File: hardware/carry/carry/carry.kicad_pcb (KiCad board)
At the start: 2 copper layers, 65 parts, among them J1 LEFT IN, J2 RIGHT IN, J3 LEFT OUT, J4 RIGHT OUT, J5 694106301002, J6 Conn_02x22_Odd_Even, J7 JST XH, U1 MCP6002-E/SN, U2 MCP6002-E/SN, U3 AZ1117CH2-5.0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

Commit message: routing carry board
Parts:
- added C26: 100n, Capacitor_SMD:C_0603_1608Metric, F.Cu at (113.0, 37.0)
- added C27: 100n, Capacitor_SMD:C_0603_1608Metric, F.Cu at (113.0, 44.0)
- added C28: 100n, Capacitor_SMD:C_0603_1608Metric, F.Cu at (132.0, 44.0)
- added H2: MountingHole_Pad, MountingHole:MountingHole_3.2mm_M3_Pad_Via, F.Cu at (44.0, 34.0)
- added H3: MountingHole_Pad, MountingHole:MountingHole_3.2mm_M3_Pad_Via, F.Cu at (136.0, 34.0)
- added H4: MountingHole_Pad, MountingHole:MountingHole_3.2mm_M3_Pad_Via, F.Cu at (136.0, 96.0)
- added H5: MountingHole_Pad, MountingHole:MountingHole_3.2mm_M3_Pad_Via, F.Cu at (44.0, 96.0)
- added J8: Conn_01x06, Connector_PinSocket_2.54mm:PinSocket_1x06_P2.54mm_Vertical, F.Cu at (83.0, 33.0)
- added R20: 100k, Resistor_SMD:R_0603_1608Metric, F.Cu at (114.0, 34.0)
- added R21: 100k, Resistor_SMD:R_0603_1608Metric, F.Cu at (112.0, 34.0)
- added R22: 100k, Resistor_SMD:R_0603_1608Metric, F.Cu at (114.0, 47.0)
- added R23: 100k, Resistor_SMD:R_0603_1608Metric, F.Cu at (112.0, 47.0)
- added R24: 100k, Resistor_SMD:R_0603_1608Metric, F.Cu at (131.0, 47.0)
- added R25: 100k, Resistor_SMD:R_0603_1608Metric, F.Cu at (133.0, 47.0)
- added R26: 2.2k, Resistor_SMD:R_0603_1608Metric, F.Cu at (77.2, 39.8)
- added R27: 2.2k, Resistor_SMD:R_0603_1608Metric, F.Cu at (79.6, 40.6)
- added SW1: RotaryEncoder_Switch, Rotary_Encoder:RotaryEncoder_Alps_EC12E-Switch_Vertical_H20mm_CircularMountingHoles, F.Cu at (120.0, 47.5)
- moved R9 47.2 mm to (87.0, 69.4), turned to 90 degrees
- moved C10 46.1 mm to (90.2, 69.4), turned to -90 degrees
- moved R10 44.8 mm to (88.6, 69.4), turned to -90 degrees
- moved C1 36.3 mm to (101.6, 88.3), turned to 0 degrees
- moved R2 35.8 mm to (101.6, 90.0), turned to 180 degrees
- moved R1 35.6 mm to (101.6, 91.7), turned to 180 degrees
- moved C4 35.5 mm to (101.6, 93.4), turned to 0 degrees
- moved D3 33.9 mm to (111.9, 52.4), turned to -90 degrees
- moved C2 32.8 mm to (98.5, 90.0), turned to 180 degrees
- moved R4 31.1 mm to (98.4, 91.7), turned to 180 degrees
- moved C3 31.0 mm to (98.4, 93.4), turned to 180 degrees
- moved R3 30.5 mm to (98.5, 88.3), turned to 0 degrees
- moved C23 30.2 mm to (93.0, 66.0), turned to 90 degrees
- moved C15 28.0 mm to (84.4, 78.0)
- moved C5 27.1 mm to (94.7, 87.4), turned to 180 degrees
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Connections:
- J6 pad 11: /DSP SOM Slot/ADC3_IN2 -> /DSP SOM Slot/ENC_A
- J6 pad 13: /DSP SOM Slot/ADC3_IN3 -> /DSP SOM Slot/ENC_B
- J6 pad 3: /DSP SOM Slot/PB10 -> /DSP SOM Slot/OLED_SCL
- J6 pad 37: /Analog Back-End/CODEC_OUT_L -> /Analog Back-End/CODEC_OUT_R
- J6 pad 39: /Analog Back-End/CODEC_OUT_R -> /Analog Back-End/CODEC_OUT_L
- J6 pad 41: /Analog Front-End/CODEC_L_IN -> /Analog Front-End/CODEC_R_IN
- J6 pad 43: /Analog Front-End/CODEC_R_IN -> /Analog Front-End/CODEC_L_IN
- J6 pad 5: /DSP SOM Slot/PB11 -> /DSP SOM Slot/OLED_SDA
- J6 pad 7: /DSP SOM Slot/PD12 -> /DSP SOM Slot/OLED_RST
- J6 pad 9: /DSP SOM Slot/PD13 -> /DSP SOM Slot/ENC_PB
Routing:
- net Net-(D1-A2): track 0.00 -> 106.4 mm
- net Net-(D4-A2): track 0.00 -> 69.4 mm, vias 0 -> 1
- net /DSP SOM Slot/ENC_B: track 0.00 -> 66.2 mm, vias 0 -> 1
- net /Analog Back-End/VREF: track 0.00 -> 63.0 mm
- net Net-(D3-A2): track 0.00 -> 56.7 mm, vias 0 -> 1
- net /DSP SOM Slot/ENC_PB: track 0.00 -> 50.7 mm, vias 0 -> 1
- net +5V: track 0.00 -> 50.4 mm
- net /DSP SOM Slot/ENC_A: track 0.00 -> 43.5 mm, vias 0 -> 1
- net Net-(D2-A2): track 0.00 -> 42.0 mm
- net /Analog Back-End/CODEC_OUT_L: track 0.00 -> 37.1 mm
- net GND: track 0.00 -> 35.7 mm, vias 0 -> 32
- net /Analog Front-End/CODEC_L_IN: track 0.00 -> 29.7 mm
- net +3.3VA: track 0.00 -> 26.0 mm, vias 0 -> 4
- net /DSP SOM Slot/OLED_RST: track 0.00 -> 25.1 mm
- net /DSP SOM Slot/OLED_SDA: track 0.00 -> 20.9 mm
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- added copper zone on F.Cu, net +3.3V
- added copper zone on F.Cu, net +3.3VA
- added copper zone on F.Cu, net +5V
- added copper zone on F.Cu, net /Power Supply/9V_CONNECTOR
- added copper zone on F.Cu, net /Power Supply/9V_FILT
- added copper zone on B.Cu, net GND
- added copper zone on F.Cu, net GND
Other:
- board outline added: 100 x 70 mm

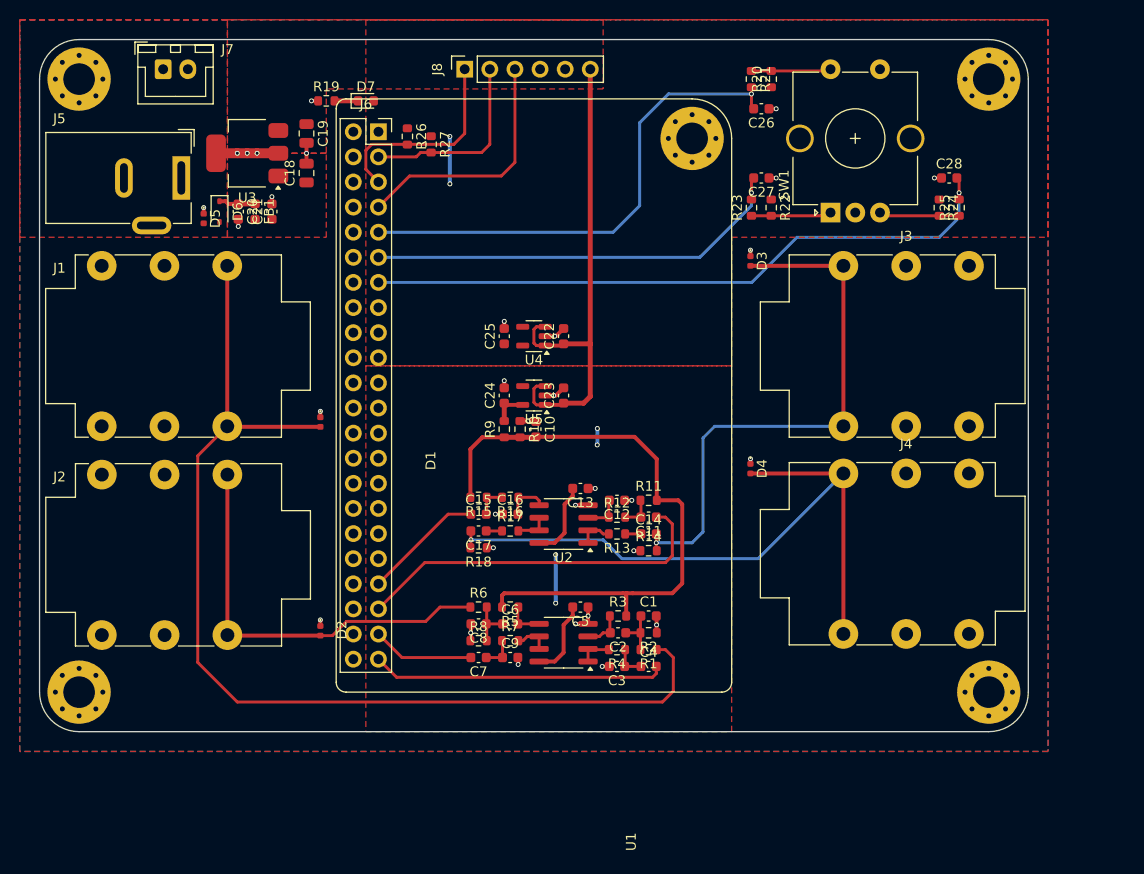
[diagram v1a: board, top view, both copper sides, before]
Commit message: carry board silkscreen
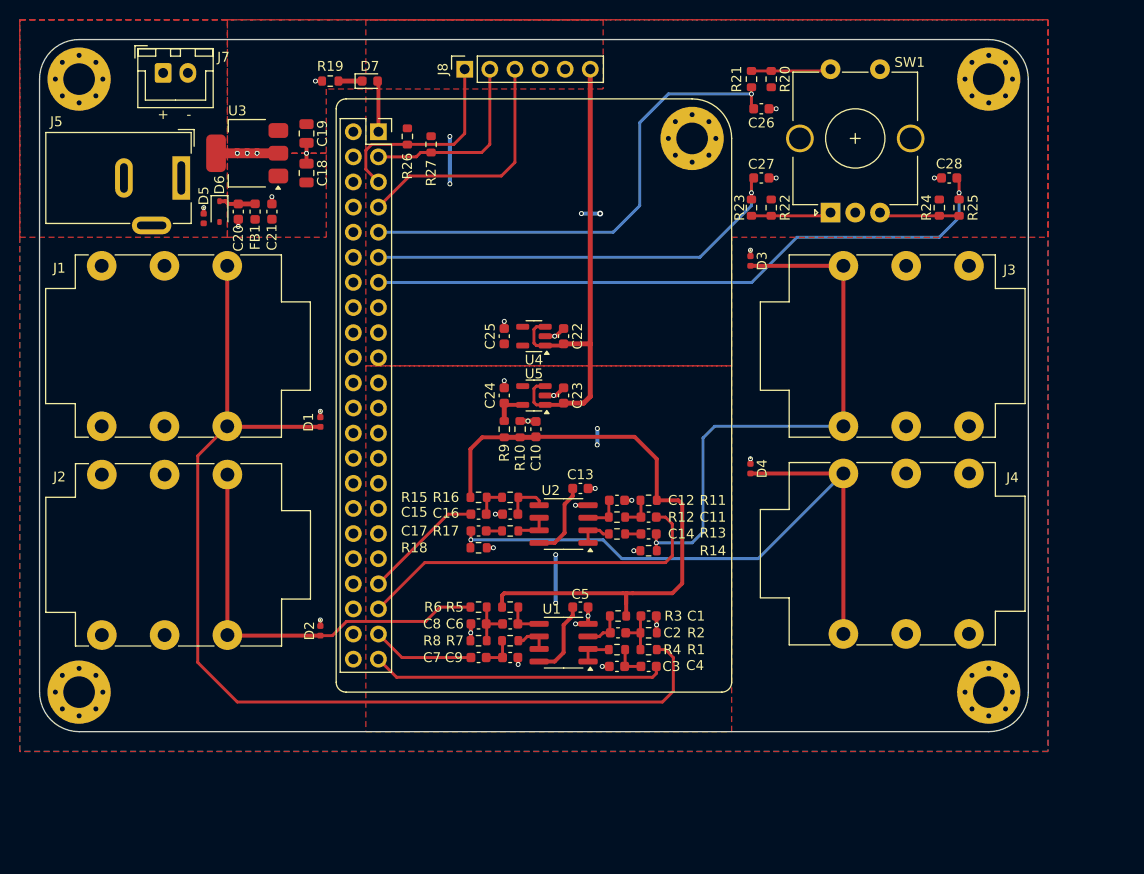
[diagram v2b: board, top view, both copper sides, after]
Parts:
- moved D7 2.04 mm to (73.4, 34.2)
- moved R19 2.04 mm to (69.4, 34.2)
- moved J7 0.38 mm to (52.5, 33.4)
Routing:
- net +3.3V: track 4.80 -> 11.9 mm, vias 2 -> 4
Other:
- board text added: "+"
- board text added: "-"

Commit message: fab files for carry board
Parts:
- added D8: LED_Small, LED_SMD:LED_0603_1608Metric, F.Cu at (101.9, 34.2)
- added R28: 1k, Resistor_SMD:R_0603_1608Metric, F.Cu at (105.2, 34.2)
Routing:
- net /DSP SOM Slot/ADC3_IN13: track 0.00 -> 49.7 mm, vias 0 -> 1
- net Net-(D8-K): track 0.00 -> 1.69 mm
- net GND: track 35.7 -> 36.4 mm, vias 32 -> 33
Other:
- board text added: "WITNS DSP SOM CARRY BOARD rev1.0 13/10/2025 Laurent Fiack"

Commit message: bom
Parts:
- D6: value BAT165A -> NSR1020MW2T1G
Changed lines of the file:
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@@
 			)
 		)
-		(property "Value" "BAT165A"
+		(property "Value" "NSR1020MW2T1G "
 			(at 0.1 1.9 90)
 			(layer "F.Fab")
